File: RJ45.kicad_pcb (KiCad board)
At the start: 2 copper layers, 19.1 x 34.9 mm, 3 parts, among them J1 Conn_01x06, J2 RJ45_Amphenol_RJMG1BD3B8K1ANR, J3 Conn_01x06

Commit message: Route tracks.
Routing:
- net Net-(J1-Pad4): track 0.00 -> 32.5 mm
- net Net-(J1-Pad5): track 0.00 -> 23.9 mm
- net Net-(J2-PadR3): track 0.00 -> 23.7 mm
- net Net-(J2-PadL1): track 0.00 -> 22.3 mm
- net Net-(J1-Pad1): track 0.00 -> 21.1 mm
- net Net-(J2-PadL2): track 0.00 -> 19.8 mm
- net Net-(J2-PadR5): track 0.00 -> 19.5 mm
- net Net-(J1-Pad6): track 0.00 -> 18.6 mm
- net Net-(J1-Pad2): track 0.00 -> 17.0 mm
- net Net-(J2-PadR6): track 0.00 -> 13.9 mm
- net Net-(J1-Pad3): track 0.00 -> 13.4 mm
- net GND: track 0.00 -> 11.0 mm
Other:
- net class Skinny added: clearance 0.1524, trace_width 0.1524, via_dia 0.6, via_drill 0.4
- rule trace_min: 0.2 -> 0.1524
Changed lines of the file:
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@@
     (thickness 1.6)
     (drawings 20)
-    (tracks 0)
+    (tracks 49)
     (zones 0)
     (modules 3)
@@
   (setup
     (last_trace_width 0.25)
+    (user_trace_width 0.1524)
     (trace_clearance 0.2)
     (zone_clearance 0.508)
     (zone_45_only no)
-    (trace_min 0.2)
+    (trace_min 0.1524)
     (segment_width 0.2)
     (edge_width 0.15)
@@
     (pad_to_mask_clearance 0)
     (aux_axis_origin 0 0)
-    (visible_elements FFFEF77F)
+    (visible_elements FFFEE77F)
     (pcbplotparams
       (layerselection 0x00030_80000001)
@@
     (add_net "Net-(J2-PadL1)")
     (add_net "Net-(J2-PadL2)")
+    (add_net "Net-(J2-PadR6)")
+    (add_net "Net-(J2-PadR7)")
+  )
+  (net_class Skinny ""
+    (clearance 0.1524)
+    (trace_width 0.1524)
+    (via_dia 0.6)
+    (via_drill 0.4)
+    (uvia_dia 0.3)
+    (uvia_drill 0.1)
     (add_net "Net-(J2-PadR3)")
     (add_net "Net-(J2-PadR5)")
-    (add_net "Net-(J2-PadR6)")
-    (add_net "Net-(J2-PadR7)")
   )
   (module Pin_Headers:Pin_Header_Straight_1x06_Pitch2.54mm (layer F.Cu)
@@
   (gr_line (start 147.955 110.49) (end 147.955 92.075) (angle 90) (layer Edge.Cuts) (width 0.15))
   (gr_line (start 128.905 110.49) (end 147.955 110.49) (angle 90) (layer Edge.Cuts) (width 0.15))
+  (segment (start 133.985 97.155) (end 133.985 95.955) (width 0.25) (layer F.Cu) (net 1))
+  (segment (start 133.985 95.955) (end 133.255001 95.225001) (width 0.25) (layer F.Cu) (net 1))
+  (segment (start 133.255001 95.225001) (end 133.255001 77.545001) (width 0.25) (layer F.Cu) (net 1))
+  (segment (start 133.255001 77.545001) (end 133.18 77.47) (width 0.25) (layer F.Cu) (net 1))
+  (segment (start 133.18 77.47) (end 132.08 77.47) (width 0.25) (layer F.Cu) (net 1))
+  (segment (start 137.795 94.615) (end 137.795 85.725) (width 0.25) (layer B.Cu) (net 2))
+  (segment (start 137.795 85.725) (end 132.08 80.01) (width 0.25) (layer B.Cu) (net 2))
+  (segment (start 135.255 94.615) (end 135.255 85.725) (width 0.25) (layer B.Cu) (net 3))
+  (segment (start 135.255 85.725) (end 132.08 82.55) (width 0.25) (layer B.Cu) (net 3))
+  (segment (start 130.655 100.445) (end 146.205 100.445) (width 0.25) (layer B.Cu) (net 4))
+  (segment (start 132.08 85.09) (end 133.35 86.36) (width 0.25) (layer B.Cu) (net 4))
+  (segment (start 133.35 86.36) (end 133.35 95.304998) (width 0.25) (layer B.Cu) (net 4))
+  (segment (start 133.35 95.304998) (end 130.655 97.999998) (width 0.25) (layer B.Cu) (net 4))
+  (segment (start 130.655 97.999998) (end 130.655 98.606523) (width 0.25) (layer B.Cu) (net 4))
+  (segment (start 130.655 98.606523) (end 130.655 100.445) (width 0.25) (layer B.Cu) (net 4))
+  (segment (start 134.665001 101.010001) (end 130.904999 97.249999) (width 0.25) (layer F.Cu) (net 5))
+  (segment (start 130.904999 97.249999) (end 130.904999 88.805001) (width 0.25) (layer F.Cu) (net 5))
+  (segment (start 130.904999 88.805001) (end 131.230001 88.479999) (width 0.25) (layer F.Cu) (net 5))
+  (segment (start 131.230001 88.479999) (end 132.08 87.63) (width 0.25) (layer F.Cu) (net 5))
+  (segment (start 132.105 108.395) (end 132.105 107.058569) (width 0.25) (layer F.Cu) (net 5))
+  (segment (start 132.105 107.058569) (end 134.665001 104.498568) (width 0.25) (layer F.Cu) (net 5))
+  (segment (start 134.665001 104.498568) (end 134.665001 101.010001) (width 0.25) (layer F.Cu) (net 5))
+  (segment (start 134.645 106.875) (end 135.589999 105.930001) (width 0.25) (layer F.Cu) (net 6))
+  (segment (start 135.589999 105.930001) (end 135.589999 101.245001) (width 0.25) (layer F.Cu) (net 6))
+  (segment (start 135.589999 101.245001) (end 132.08 97.735002) (width 0.25) (layer F.Cu) (net 6))
+  (segment (start 132.08 97.735002) (end 132.08 91.372081) (width 0.25) (layer F.Cu) (net 6))
+  (segment (start 132.08 91.372081) (end 132.08 90.17) (width 0.25) (layer F.Cu) (net 6))
+  (segment (start 136.525 97.155) (end 136.525 84.7226) (width 0.1524) (layer F.Cu) (net 7))
+  (segment (start 136.525 84.7226) (end 143.7776 77.47) (width 0.1524) (layer F.Cu) (net 7))
+  (segment (start 143.7776 77.47) (end 144.78 77.47) (width 0.1524) (layer F.Cu) (net 7))
+  (segment (start 139.065 97.155) (end 139.065 85.725) (width 0.1524) (layer F.Cu) (net 8))
+  (segment (start 139.065 85.725) (end 144.78 80.01) (width 0.1524) (layer F.Cu) (net 8))
+  (segment (start 140.335 94.615) (end 140.335 86.995) (width 0.25) (layer F.Cu) (net 9))
+  (segment (start 140.335 86.995) (end 144.78 82.55) (width 0.25) (layer F.Cu) (net 9))
+  (segment (start 144.78 85.09) (end 143.577919 85.09) (width 0.25) (layer F.Cu) (net 11))
+  (segment (start 142.875 93.271498) (end 142.875 94.615) (width 0.25) (layer F.Cu) (net 11))
+  (segment (start 143.577919 85.09) (end 142.875 85.792919) (width 0.25) (layer F.Cu) (net 11))
+  (segment (start 142.875 85.792919) (end 142.875 93.271498) (width 0.25) (layer F.Cu) (net 11))
+  (segment (start 145.629999 88.479999) (end 144.78 87.63) (width 0.25) (layer F.Cu) (net 12))
+  (segment (start 145.955001 88.805001) (end 145.629999 88.479999) (width 0.25) (layer F.Cu) (net 12))
+  (segment (start 142.194999 99.106411) (end 145.955001 95.346409) (width 0.25) (layer F.Cu) (net 12))
+  (segment (start 142.194999 104.314999) (end 142.194999 99.106411) (width 0.25) (layer F.Cu) (net 12))
+  (segment (start 144.755 106.875) (end 142.194999 104.314999) (width 0.25) (layer F.Cu) (net 12))
+  (segment (start 145.955001 95.346409) (end 145.955001 88.805001) (width 0.25) (layer F.Cu) (net 12))
+  (segment (start 141.605 99.06) (end 144.78 95.885) (width 0.25) (layer F.Cu) (net 13))
+  (segment (start 144.78 95.885) (end 144.78 90.17) (width 0.25) (layer F.Cu) (net 13))
+  (segment (start 141.605 106.448569) (end 141.605 99.06) (width 0.25) (layer F.Cu) (net 13))
+  (segment (start 142.215 108.395) (end 142.215 107.058569) (width 0.25) (layer F.Cu) (net 13))
+  (segment (start 142.215 107.058569) (end 141.605 106.448569) (width 0.25) (layer F.Cu) (net 13))
 )

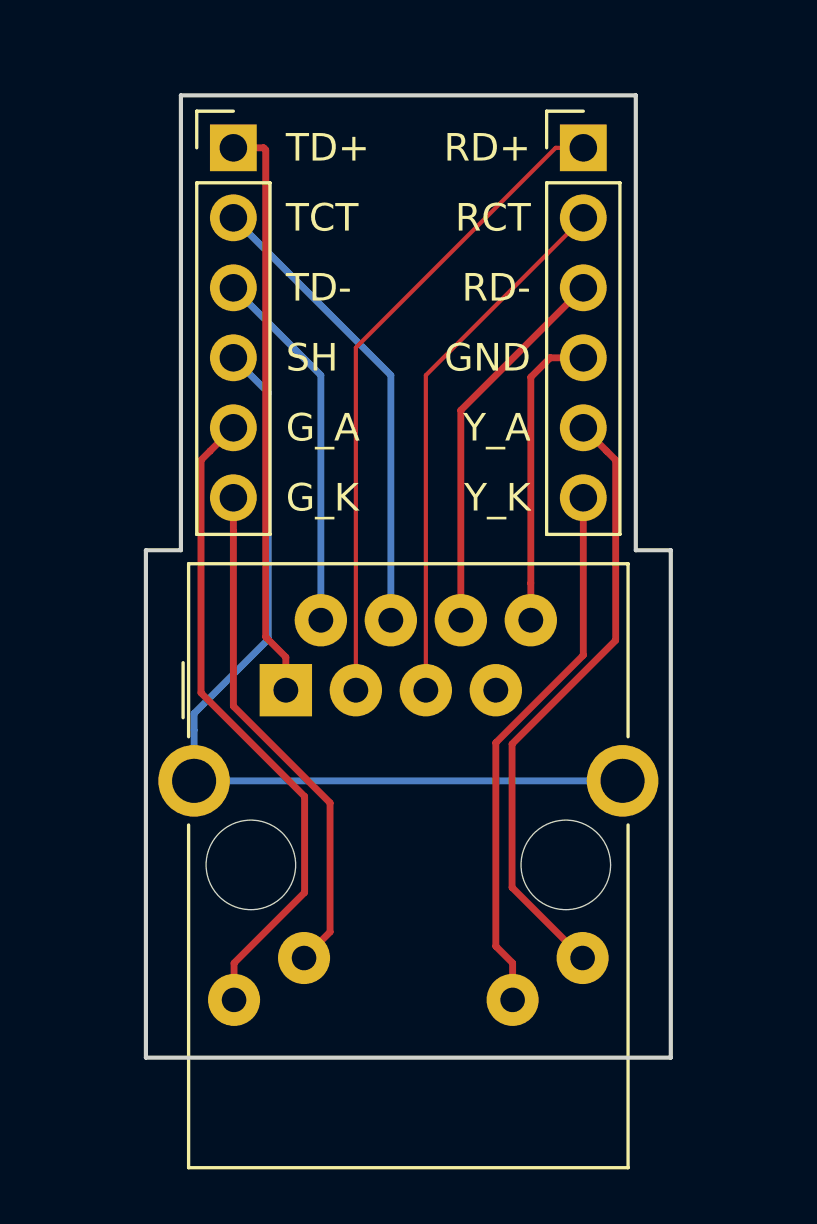
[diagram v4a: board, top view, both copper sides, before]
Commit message: Add filled zones.
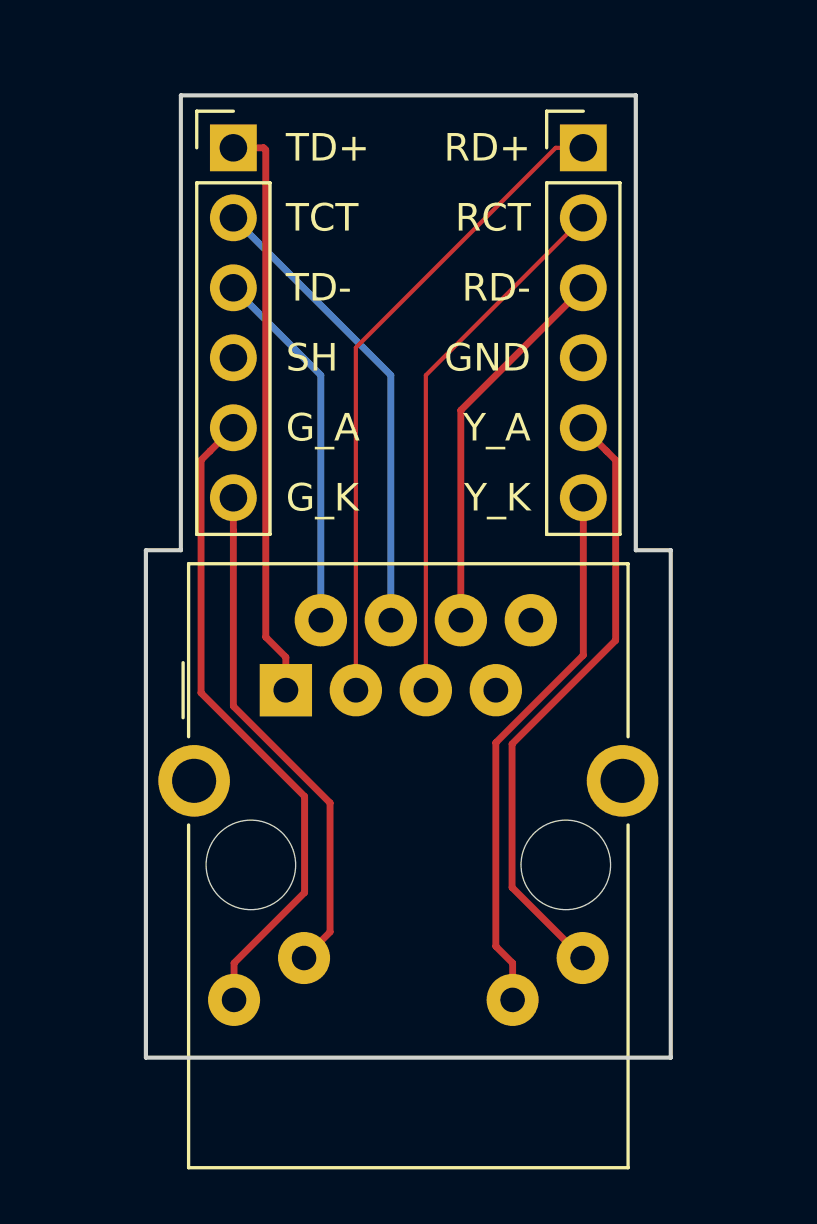
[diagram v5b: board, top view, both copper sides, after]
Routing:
- net Net-(J1-Pad4): track 32.5 -> 0.00 mm
- net GND: track 11.0 -> 0.00 mm
- added copper zone on F.Cu, net GND
- added copper zone on B.Cu, net Net-(J1-Pad4)
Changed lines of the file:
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@@
   (general
     (links 13)
-    (no_connects 13)
+    (no_connects 3)
     (area 0 0 0 0)
     (thickness 1.6)
     (drawings 20)
-    (tracks 49)
+    (tracks 39)
     (zones 0)
     (modules 3)
@@
     (user_trace_width 0.1524)
     (trace_clearance 0.2)
-    (zone_clearance 0.508)
+    (zone_clearance 0.3048)
     (zone_45_only no)
     (trace_min 0.1524)
@@
     (pad_to_mask_clearance 0)
     (aux_axis_origin 0 0)
-    (visible_elements FFFEE77F)
+    (visible_elements FFFEF77F)
     (pcbplotparams
       (layerselection 0x00030_80000001)
@@
   (segment (start 135.255 94.615) (end 135.255 85.725) (width 0.25) (layer B.Cu) (net 3))
   (segment (start 135.255 85.725) (end 132.08 82.55) (width 0.25) (layer B.Cu) (net 3))
-  (segment (start 130.655 100.445) (end 146.205 100.445) (width 0.25) (layer B.Cu) (net 4))
-  (segment (start 132.08 85.09) (end 133.35 86.36) (width 0.25) (layer B.Cu) (net 4))
-  (segment (start 133.35 86.36) (end 133.35 95.304998) (width 0.25) (layer B.Cu) (net 4))
-  (segment (start 133.35 95.304998) (end 130.655 97.999998) (width 0.25) (layer B.Cu) (net 4))
-  (segment (start 130.655 97.999998) (end 130.655 98.606523) (width 0.25) (layer B.Cu) (net 4))
-  (segment (start 130.655 98.606523) (end 130.655 100.445) (width 0.25) (layer B.Cu) (net 4))
   (segment (start 134.665001 101.010001) (end 130.904999 97.249999) (width 0.25) (layer F.Cu) (net 5))
   (segment (start 130.904999 97.249999) (end 130.904999 88.805001) (width 0.25) (layer F.Cu) (net 5))
@@
   (segment (start 140.335 94.615) (end 140.335 86.995) (width 0.25) (layer F.Cu) (net 9))
   (segment (start 140.335 86.995) (end 144.78 82.55) (width 0.25) (layer F.Cu) (net 9))
-  (segment (start 144.78 85.09) (end 143.577919 85.09) (width 0.25) (layer F.Cu) (net 11))
-  (segment (start 142.875 93.271498) (end 142.875 94.615) (width 0.25) (layer F.Cu) (net 11))
-  (segment (start 143.577919 85.09) (end 142.875 85.792919) (width 0.25) (layer F.Cu) (net 11))
-  (segment (start 142.875 85.792919) (end 142.875 93.271498) (width 0.25) (layer F.Cu) (net 11))
   (segment (start 145.629999 88.479999) (end 144.78 87.63) (width 0.25) (layer F.Cu) (net 12))
   (segment (start 145.955001 88.805001) (end 145.629999 88.479999) (width 0.25) (layer F.Cu) (net 12))
@@
   (segment (start 142.215 108.395) (end 142.215 107.058569) (width 0.25) (layer F.Cu) (net 13))
   (segment (start 142.215 107.058569) (end 141.605 106.448569) (width 0.25) (layer F.Cu) (net 13))
+  (zone (net 4) (net_name "Net-(J1-Pad4)") (layer B.Cu) (hatch edge 0.508)
+    (connect_pads (clearance 0.3048))
+    (min_thickness 0.254)
+    (fill (arc_segments 16) (thermal_gap 0.508) (thermal_bridge_width 0.508))
+    (polygon
+      (pts
+        (xy 146.685 92.075) (xy 147.955 92.075) (xy 147.955 110.49) (xy 128.905 110.49) (xy 128.905 92.075)
+        (xy 130.175 92.075) (xy 130.175 75.565) (xy 146.685 75.565)
+      )
+    )
+  )
+  (zone (net 11) (net_name GND) (layer F.Cu) (hatch edge 0.508)
+    (connect_pads (clearance 0.3048))
+    (min_thickness 0.254)
+    (fill (arc_segments 16) (thermal_gap 0.508) (thermal_bridge_width 0.508))
+    (polygon
+      (pts
+        (xy 146.685 92.075) (xy 147.955 92.075) (xy 147.955 110.49) (xy 128.905 110.49) (xy 128.905 92.075)
+        (xy 130.175 92.075) (xy 130.175 75.565) (xy 146.685 75.565)
+      )
+    )
+  )
 )
